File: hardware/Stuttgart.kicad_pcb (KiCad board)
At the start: 2 copper layers, 70 x 70 mm, 79 parts, among them IC1 NCV1117ST33T3G, IC2 UCC12040DVER, IC3 MCP1700T-3302E_TT, IC4 ISO7763DBQR, IC5 ISO7741DBQR, IC6 MCP3202-CI_SN, IC7 MCP251863T-E_9PX, J1 USB_C_Receptacle_USB2.0_16P, J2 FCR7350B, J3 FCR7350G, J4 FCR7350Y, J5 SM03B-SRSS-TB_LF__SN_, U1 RP2354A, Y1 ABM8-272-T3, Y2 Crystal_GND24

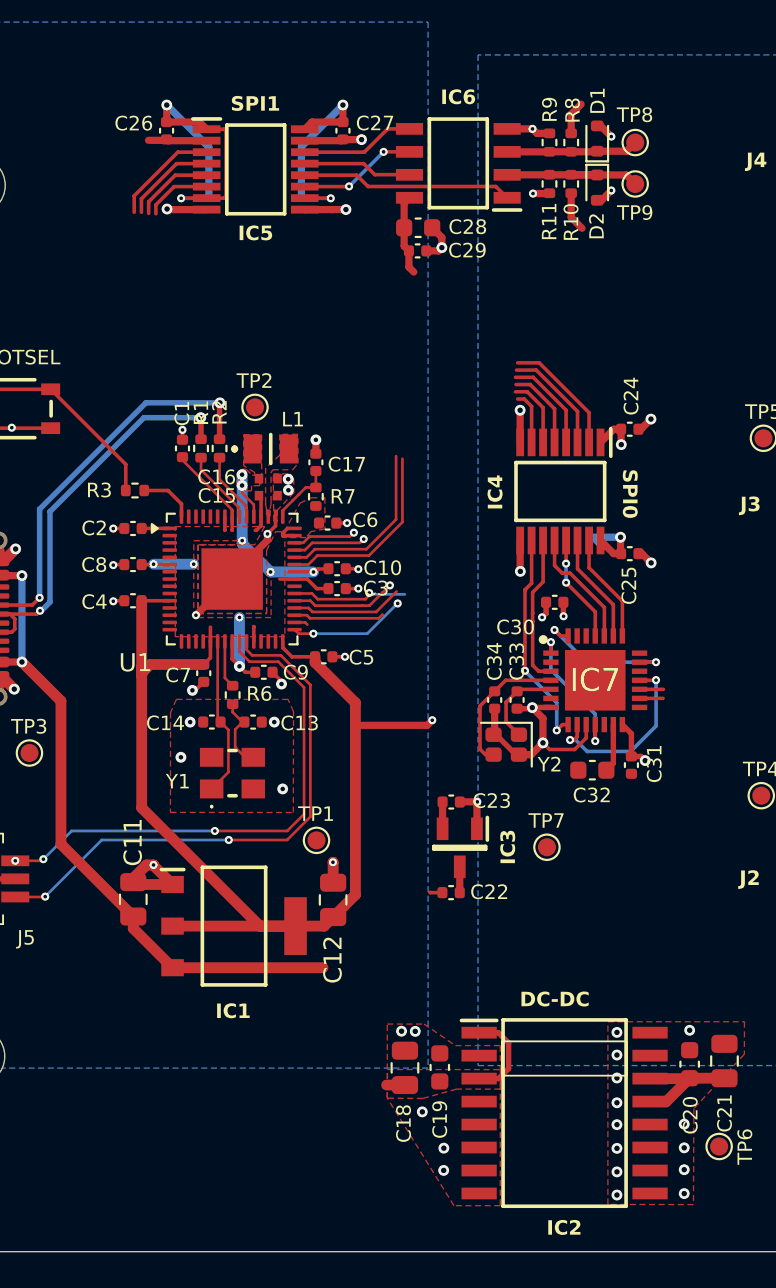
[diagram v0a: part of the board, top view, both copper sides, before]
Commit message: Added new DCDC to library
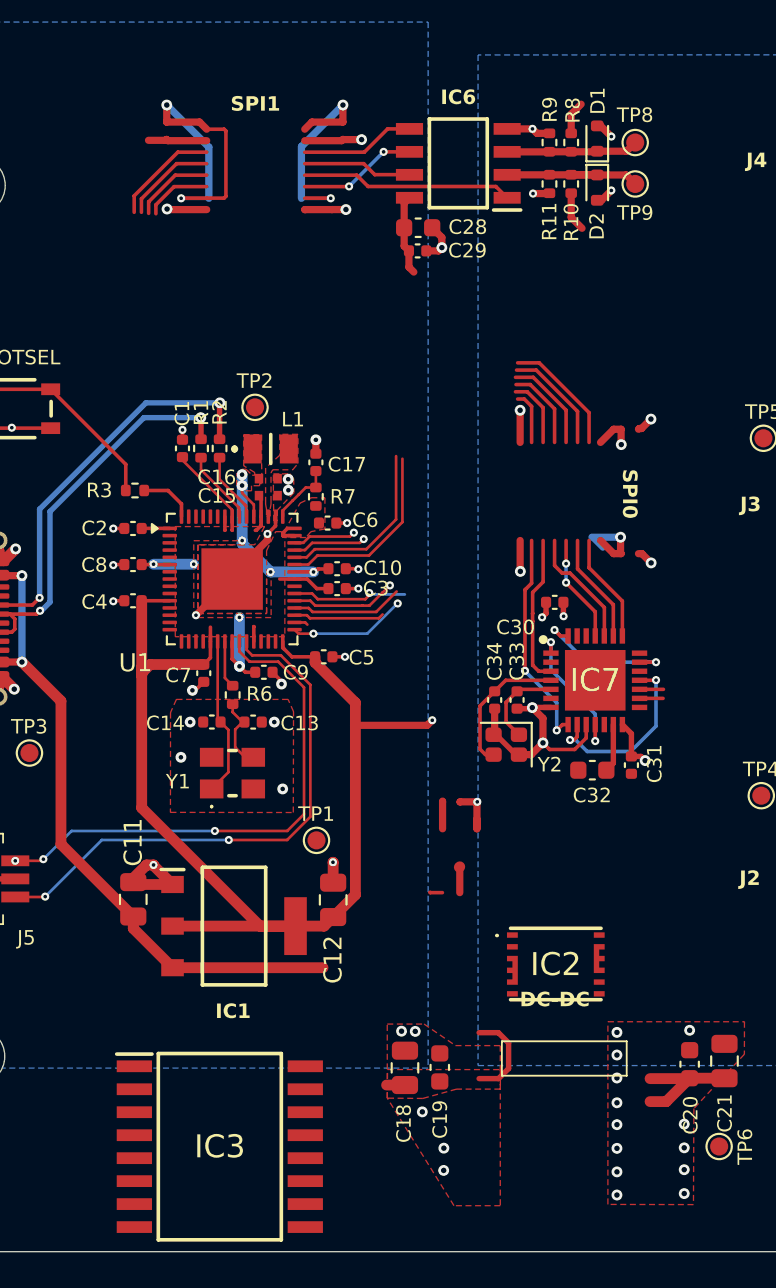
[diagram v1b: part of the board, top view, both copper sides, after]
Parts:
- removed C22, C23: 1u, Capacitor_SMD:C_0402_1005Metric
- removed C24, C25, C26, C27: 100n, Capacitor_SMD:C_0402_1005Metric
- removed IC4: ISO7763DBQR, Stuttgart:SOP64P600X175-16N
- removed IC5: ISO7741DBQR, Stuttgart:SOP64P600X175-16N
- removed TP7: TestPoint, TestPoint:TestPoint_Pad_D1.0mm
- IC2: value UCC12040DVER -> UCC33420QRAQRQ1; footprint Stuttgart:SOIC127P1030X265-16N -> Stuttgart:UCC33020QRAQRQ1
- IC3: value MCP1700T-3302E_TT -> ISOUSB111DWR; footprint Stuttgart:SOT95P237X112-3N -> Stuttgart:SOIC127P1030X265-16N
- moved IC3 21.2 mm to (122.0, 109.7), turned to 0 degrees
- moved IC2 8.23 mm to (140.5, 99.6)
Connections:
- IC2 pad 1: VBUS -> unconnected-(IC2-EN/FLT-Pad1)
- IC2 pad 10: GND1 -> unconnected-(IC2-GNDS_2-Pad10)
- IC2 pad 11: GND1 -> unconnected-(IC2-GNDS_3-Pad11)
- IC2 pad 12: GND1 -> unconnected-(IC2-GNDS_4-Pad12)
- IC2 pad 13: +5V -> unconnected-(IC2-GNDP_5-Pad13)
- IC2 pad 14: +5V -> unconnected-(IC2-GNDS_5-Pad14)
- IC2 pad 2: GND -> unconnected-(IC2-VINP-Pad2)
- IC2 pad 3: VBUS -> unconnected-(IC2-GNDP_1-Pad3)
- IC2 pad 4: GND -> unconnected-(IC2-GNDP_2-Pad4)
- IC2 pad 6: GND -> unconnected-(IC2-GNDP_4-Pad6)
- IC2 pad 7: GND -> unconnected-(IC2-SEL-Pad7)
- IC2 pad 8: GND -> unconnected-(IC2-VCC-Pad8)
- IC2 pad 9: GND1 -> unconnected-(IC2-GNDS_1-Pad9)
- IC3 pad 1: GND1 -> unconnected-(IC3-VBUS1-Pad1)
- IC3 pad 2: +3.3VA -> GND
- IC3 pad 3: +5V -> unconnected-(IC3-V3P3V1-Pad3)

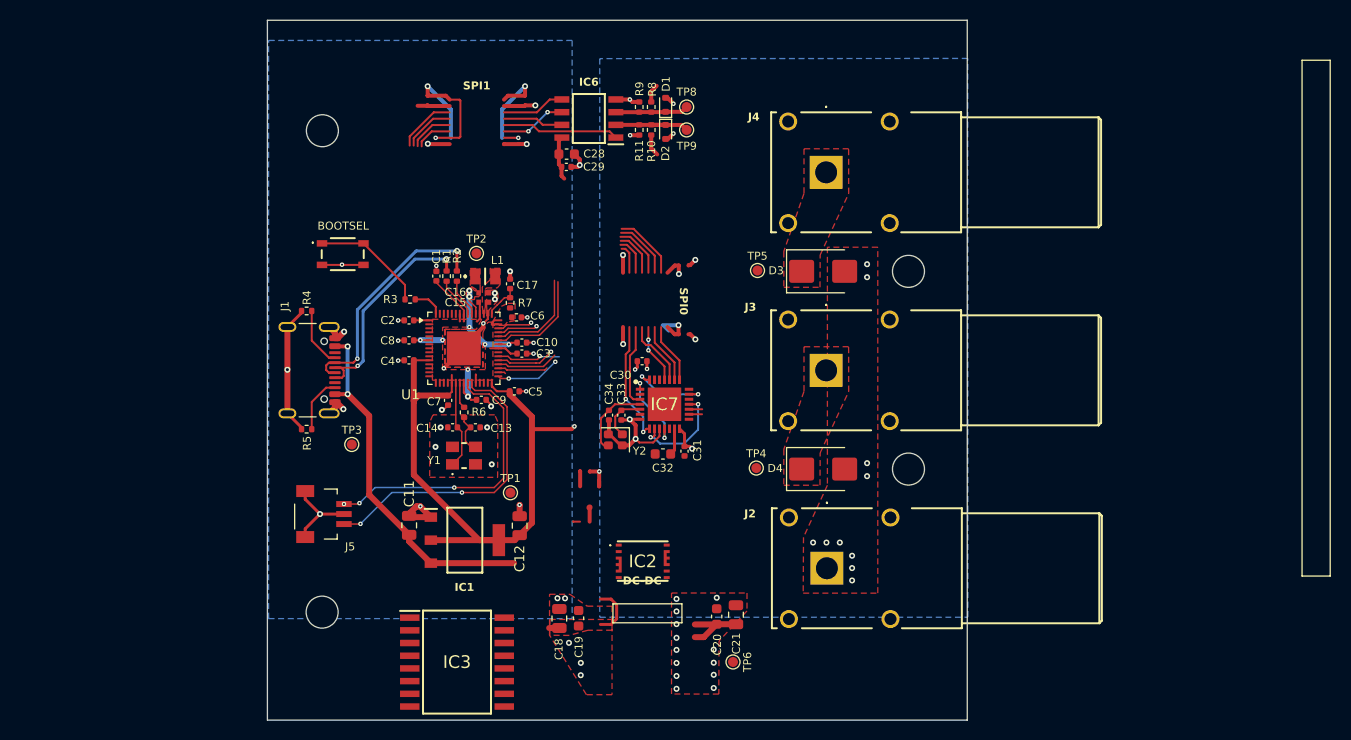
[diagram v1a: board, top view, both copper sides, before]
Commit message: Moved GND points, revised DCDC and base USB Work
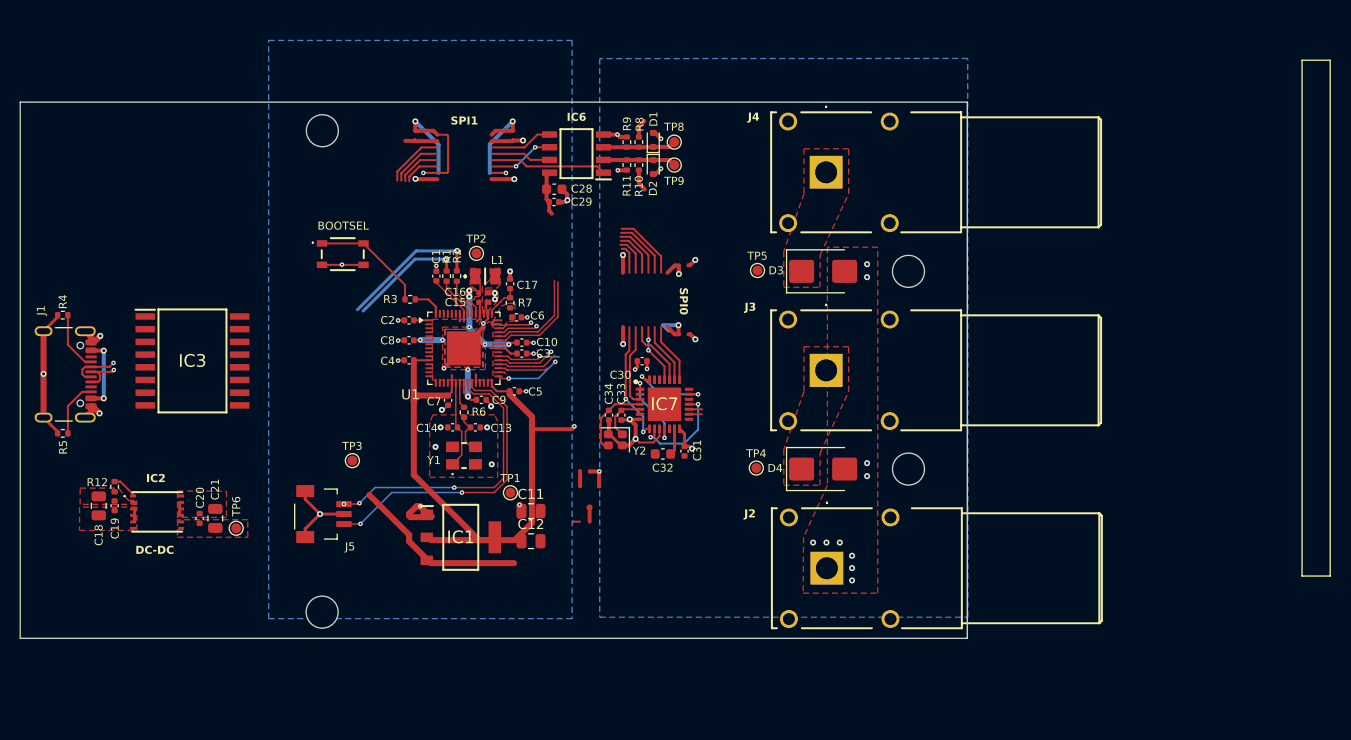
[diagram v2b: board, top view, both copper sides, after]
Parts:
- added R12: 18k, Resistor_SMD:R_0402_1005Metric, F.Cu at (87.7, 92.2)
- C19, C20: value 100n -> 15n; footprint Capacitor_SMD:C_0603_1608Metric -> Capacitor_SMD:C_0402_1005Metric
- C21: value 10u -> 22u
- moved C21 53.0 mm to (97.8, 95.3)
- moved C20 52.6 mm to (96.2, 95.3)
- moved TP6 51.5 mm to (99.9, 96.3)
- moved IC2 48.8 mm to (92.0, 94.7)
- moved C19 47.7 mm to (87.7, 94.1), turned to -90 degrees
- moved C18 47.4 mm to (86.1, 94.1), turned to -90 degrees
- moved IC3 40.1 mm to (95.5, 79.6)
- moved J1 24.4 mm to (81.7, 80.9)
- moved R4 24.4 mm to (82.5, 75.0)
- moved R5 24.4 mm to (82.5, 86.8)
- moved C11 12.3 mm to (129.4, 94.6), turned to 0 degrees
- moved IC6 3.72 mm to (133.9, 58.8)
- moved C28 3.72 mm to (131.7, 62.4)
- moved C29 3.72 mm to (131.7, 63.7)
- moved D1 3.72 mm to (141.6, 57.5)
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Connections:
- C1 pad 2: GND -> GND1
- C10 pad 2: GND -> GND1
- C13 pad 2: GND -> GND1
- C14 pad 1: GND -> GND1
- C15 pad 2: GND -> GND1
- C16 pad 2: GND -> GND1
- C17 pad 2: GND -> GND1
- C2 pad 2: GND -> GND1
- C3 pad 2: GND -> GND1
- C4 pad 2: GND -> GND1
- C5 pad 2: GND -> GND1
- C6 pad 2: GND -> GND1
- C7 pad 2: GND -> GND1
- C8 pad 2: GND -> GND1
- C9 pad 2: GND -> GND1
- IC2 pad 1: unconnected-(IC2-EN/FLT-Pad1) -> /Power/EN
- IC2 pad 10: unconnected-(IC2-GNDS_2-Pad10) -> GND1
- IC2 pad 11: unconnected-(IC2-GNDS_3-Pad11) -> GND1
- IC2 pad 12: unconnected-(IC2-GNDS_4-Pad12) -> GND1
- IC2 pad 13: unconnected-(IC2-GNDP_5-Pad13) -> GND
- IC2 pad 14: unconnected-(IC2-GNDS_5-Pad14) -> GND1
- IC2 pad 2: unconnected-(IC2-VINP-Pad2) -> VBUS
- IC2 pad 3: unconnected-(IC2-GNDP_1-Pad3) -> GND
- IC2 pad 4: unconnected-(IC2-GNDP_2-Pad4) -> GND
- IC2 pad 5: unconnected-(IC2-GNDP_3-Pad5) -> GND
- IC2 pad 6: unconnected-(IC2-GNDP_4-Pad6) -> GND
- IC2 pad 7: unconnected-(IC2-SEL-Pad7) -> +5V
- IC2 pad 8: unconnected-(IC2-VCC-Pad8) -> +5V
- IC2 pad 9: unconnected-(IC2-GNDS_1-Pad9) -> GND1
- J5 pad 2: GND -> GND1
- J5 pad MP1: GND -> GND1
- J5 pad MP2: GND -> GND1
- S1 pad 3: GND -> GND1
- S1 pad 4: GND -> GND1
- U1 pad 47: GND -> GND1
- U1 pad 61: GND -> GND1
- Y1 pad 2: GND -> GND1
- Y1 pad 4: GND -> GND1
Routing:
- net GND: track 60.3 -> 31.9 mm, vias 34 -> 27
- net GND1: track 32.6 -> 59.9 mm, vias 36 -> 24
- net VBUS: track 42.2 -> 26.2 mm, vias 2 -> 3
- net +5V: track 11.0 -> 4.14 mm
- net USB_D+: track 22.3 -> 16.6 mm
- net USB_D-: track 24.2 -> 19.3 mm
- net /Power/EN: track 0.00 -> 2.54 mm
- added copper zone on F.Cu, net +5V
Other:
- board size 70 x 70 mm -> 94.7 x 53.6 mm

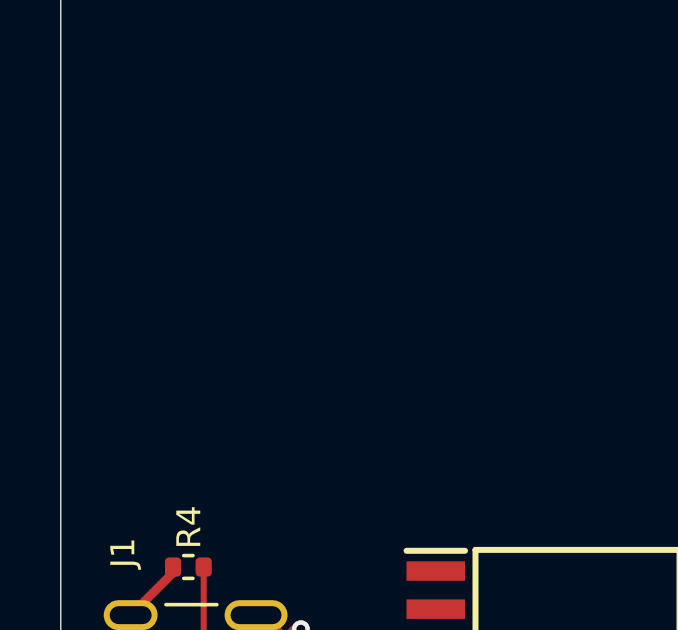
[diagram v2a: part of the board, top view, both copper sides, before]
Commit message: Improved USB Protection
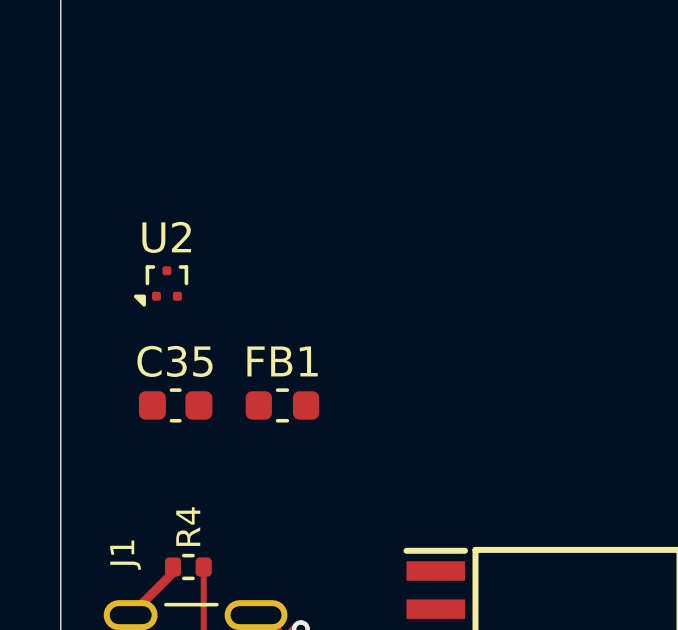
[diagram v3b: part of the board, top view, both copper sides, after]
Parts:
- added C35: 100n, Capacitor_SMD:C_0603_1608Metric, F.Cu at (82.1, 69.6)
- added FB1: FerriteBead, Inductor_SMD:L_0603_1608Metric, F.Cu at (85.7, 69.6)
- added U2: TPD2EUSB30, Package_TO_SOT_SMD:Texas_DRT-3, F.Cu at (81.8, 65.5)
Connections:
- net Net-(J1-CC1) renamed /USB Isolation/CC1
- net Net-(J1-CC2) renamed /USB Isolation/CC2
- IC3 pad 6: unconnected-(IC3-UD--Pad6) -> /USB Isolation/USB_D-
- IC3 pad 7: unconnected-(IC3-UD+-Pad7) -> /USB Isolation/USB_D+
- J1 pad A4: VBUS -> /USB Isolation/VBUS_IN
- J1 pad A6: USB_D+ -> /USB Isolation/USB_D+
- J1 pad A7: USB_D- -> /USB Isolation/USB_D-
- J1 pad A9: VBUS -> /USB Isolation/VBUS_IN
- J1 pad B4: VBUS -> /USB Isolation/VBUS_IN
- J1 pad B6: USB_D+ -> /USB Isolation/USB_D+
- J1 pad B7: USB_D- -> /USB Isolation/USB_D-
- J1 pad B9: VBUS -> /USB Isolation/VBUS_IN
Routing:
- net VBUS: track 26.2 -> 18.9 mm, vias 3 -> 1
- net /USB Isolation/VBUS_IN: track 0.00 -> 7.33 mm, vias 0 -> 2
- net USB_D+: track 16.6 -> 11.7 mm, vias 2 -> 1
- net /USB Isolation/USB_D+: track 0.00 -> 4.91 mm, vias 0 -> 1
- net /USB Isolation/USB_D-: track 0.00 -> 4.85 mm, vias 0 -> 1
- net USB_D-: track 19.3 -> 14.4 mm, vias 2 -> 1

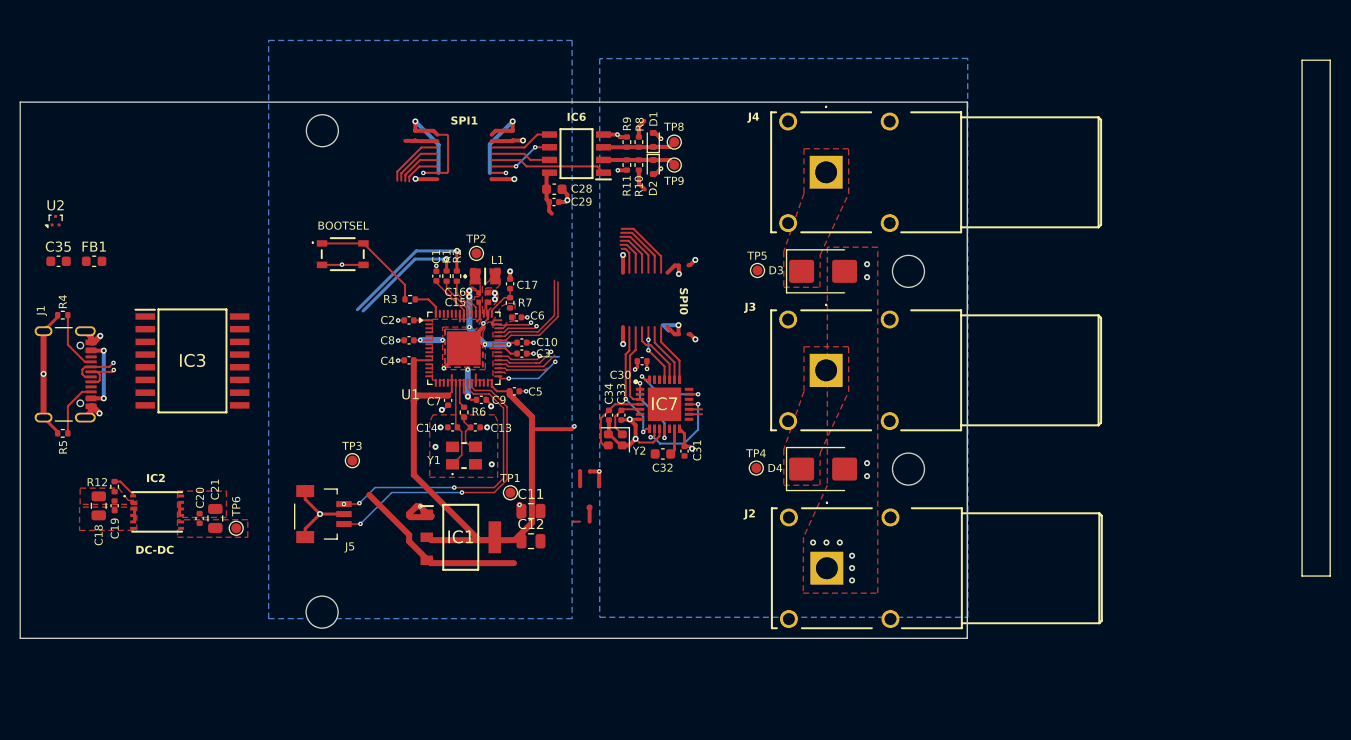
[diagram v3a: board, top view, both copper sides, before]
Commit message: Schematic complete and base components placed
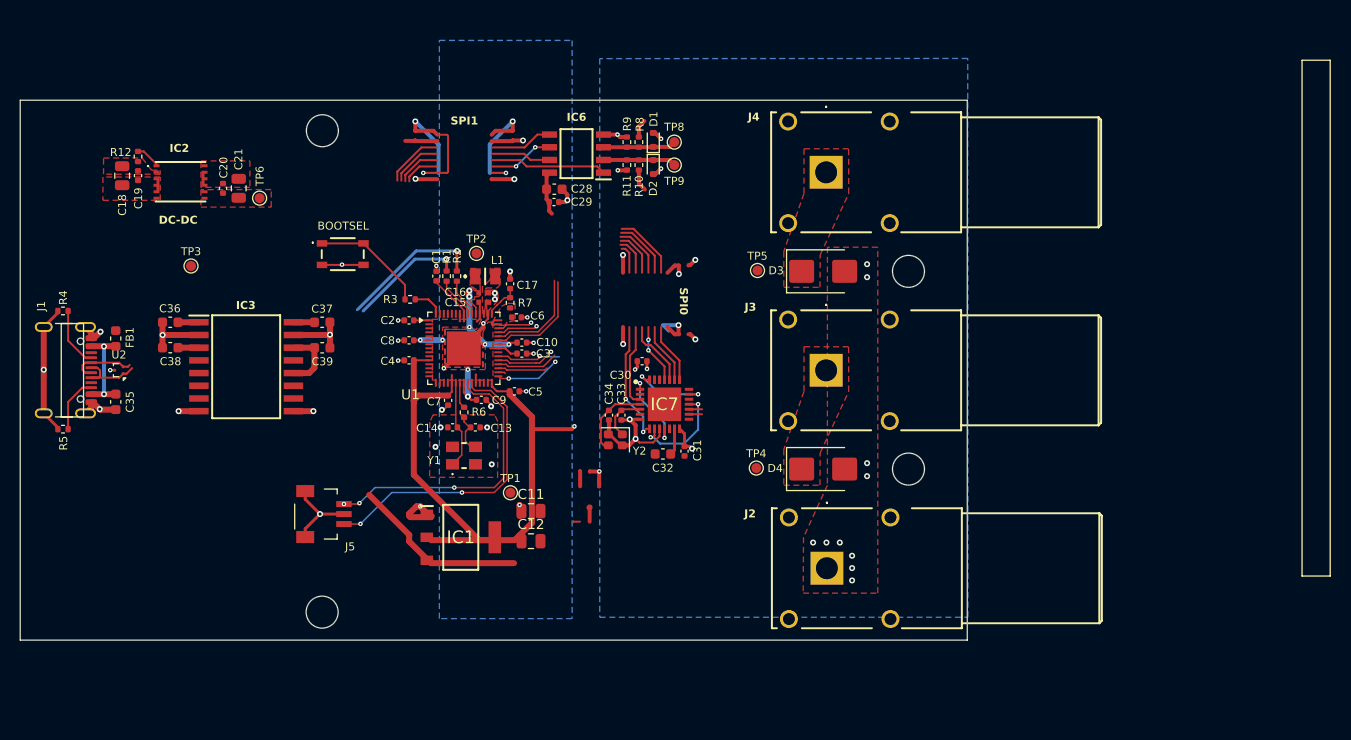
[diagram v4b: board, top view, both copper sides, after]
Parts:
- added C36: 1u, Capacitor_SMD:C_0603_1608Metric, F.Cu at (93.3, 75.7)
- added C37: 1u, Capacitor_SMD:C_0603_1608Metric, F.Cu at (108.5, 75.7)
- added C38: 0.1u, Capacitor_SMD:C_0603_1608Metric, F.Cu at (93.3, 78.2)
- added C39: 0.1u, Capacitor_SMD:C_0603_1608Metric, F.Cu at (108.5, 78.3)
- moved C19 33.1 mm to (90.1, 61.0)
- moved IC2 33.1 mm to (94.3, 61.7)
- moved R12 33.1 mm to (90.1, 59.1)
- moved TP6 33.1 mm to (102.2, 63.3)
- moved C18 33.1 mm to (88.5, 61.0)
- moved C20 33.1 mm to (98.6, 62.3)
- moved C21 33.1 mm to (100.1, 62.3)
- moved TP3 25.3 mm to (95.4, 70.1)
- moved U2 16.2 mm to (88.1, 80.5), turned to 90 degrees
- moved C35 15.2 mm to (87.8, 83.7), turned to -90 degrees
- moved FB1 8.02 mm to (87.8, 77.3), turned to 90 degrees
- moved IC3 5.40 mm to (100.9, 80.2)
- moved R4 0.42 mm to (82.6, 74.6)
- moved J1 0.42 mm to (81.7, 80.5)
- moved R5 0.42 mm to (82.6, 86.4)
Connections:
- IC3 pad 1: unconnected-(IC3-VBUS1-Pad1) -> VBUS
- IC3 pad 10: unconnected-(IC3-DD+-Pad10) -> USB_D+
- IC3 pad 11: unconnected-(IC3-DD--Pad11) -> USB_D-
- IC3 pad 12: unconnected-(IC3-PIN-Pad12) -> Net-(IC3-PIN)
- IC3 pad 14: unconnected-(IC3-V3P3V2-Pad14) -> Net-(IC3-PIN)
- IC3 pad 16: unconnected-(IC3-VBUS2-Pad16) -> +5V
- IC3 pad 3: unconnected-(IC3-V3P3V1-Pad3) -> Net-(IC3-V3P3V1)
- IC3 pad 6: /USB Isolation/USB_D- -> USB_D-
- IC3 pad 7: /USB Isolation/USB_D+ -> USB_D+
- J1 pad A6: /USB Isolation/USB_D+ -> USB_D+
- J1 pad A7: /USB Isolation/USB_D- -> USB_D-
- J1 pad B6: /USB Isolation/USB_D+ -> USB_D+
- J1 pad B7: /USB Isolation/USB_D- -> USB_D-
- U2 pad 1: /USB Isolation/USB_D+ -> USB_D+
- U2 pad 2: /USB Isolation/USB_D- -> USB_D-
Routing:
- net GND: track 31.9 -> 42.1 mm, vias 27 -> 30
- net GND1: track 59.9 -> 68.1 mm, vias 24 -> 26
- net USB_D+: track 11.7 -> 18.7 mm
- net USB_D-: track 14.4 -> 20.9 mm
- net Net-(IC3-PIN): track 0.00 -> 6.43 mm
- net /USB Isolation/USB_D+: track 4.91 -> 0.00 mm, vias 1 -> 0
- net /USB Isolation/USB_D-: track 4.85 -> 0.00 mm, vias 1 -> 0
- net /USB Isolation/VBUS_IN: track 7.33 -> 11.0 mm
- net +5V: track 4.14 -> 6.25 mm
- net VBUS: track 18.9 -> 21.0 mm
- net Net-(IC3-V3P3V1): track 0.00 -> 2.09 mm
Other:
- board size 94.7 x 53.6 mm -> 94.7 x 54 mm
